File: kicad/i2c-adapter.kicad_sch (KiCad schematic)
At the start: 40 parts, among them J1 Conn_02x13_Top_Bottom, J10 AUX IN, J11 +5V, J2 I2C-1, J3 I2C-2, J4 I2C-3R, J5 I2C-4R, J6 SPI-1, J7 SPI-2, J8 SPI-3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

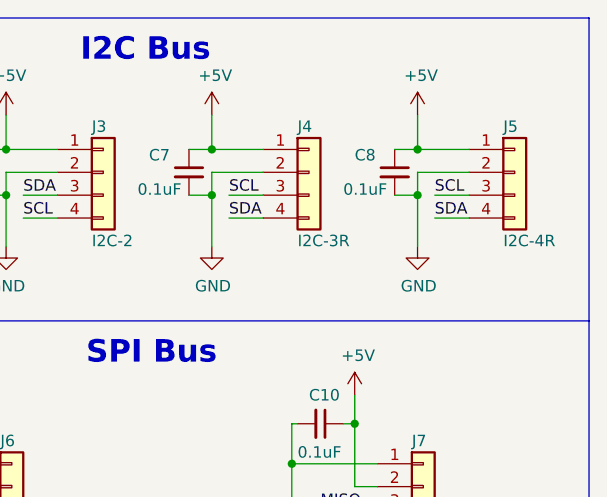
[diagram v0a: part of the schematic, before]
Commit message: Cleaned up PCB routes and positions; Converted I2C to Adafruit standard pinout. Have Git ignore Kicad generated files.
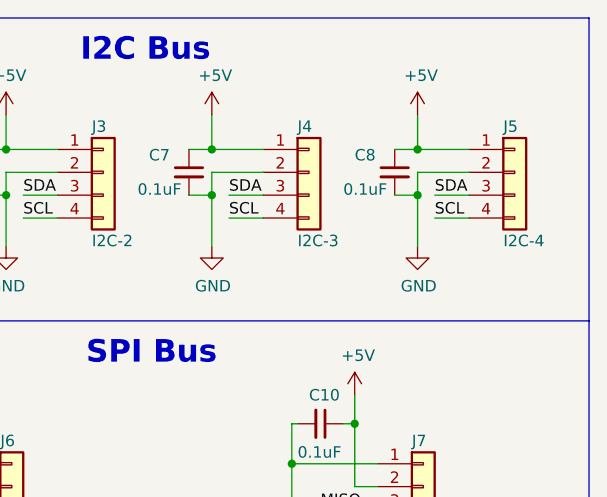
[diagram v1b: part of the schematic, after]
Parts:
- J4: value I2C-3R -> I2C-3
- J5: value I2C-4R -> I2C-4
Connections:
- net SCL: now also J4.4 (Pin_4), J5.4 (Pin_4); no longer J4.3 (Pin_3), J5.3 (Pin_3)
- net SDA: now also J4.3 (Pin_3), J5.3 (Pin_3); no longer J4.4 (Pin_4), J5.4 (Pin_4)
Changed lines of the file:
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@@
     (effects (font (size 1.27 1.27)) (justify right bottom))
   )
-  (label "SDA" (at 222.885 38.1 0)
+  (label "SCL" (at 222.885 38.1 0)
     (effects (font (size 1.27 1.27)) (justify left bottom))
   )
@@
     (effects (font (size 1.27 1.27)) (justify left bottom))
   )
-  (label "SCL" (at 245.745 35.56 0)
+  (label "SDA" (at 245.745 35.56 0)
     (effects (font (size 1.27 1.27)) (justify left bottom))
   )
@@
     (effects (font (size 1.27 1.27)) (justify left bottom))
   )
-  (label "SDA" (at 245.745 38.1 0)
+  (label "SCL" (at 245.745 38.1 0)
     (effects (font (size 1.27 1.27)) (justify left bottom))
   )
@@
     (effects (font (size 1.27 1.27)) (justify left bottom))
   )
-  (label "SCL" (at 222.885 35.56 0)
+  (label "SDA" (at 222.885 35.56 0)
     (effects (font (size 1.27 1.27)) (justify left bottom))
   )
@@
       (effects (font (size 1.27 1.27)) (justify left))
     )
-    (property "Value" "I2C-3R" (id 1) (at 230.505 40.64 0)
+    (property "Value" "I2C-3" (id 1) (at 230.505 40.64 0)
       (effects (font (size 1.27 1.27)) (justify left))
     )
@@
       (effects (font (size 1.27 1.27)) (justify left))
     )
-    (property "Value" "I2C-4R" (id 1) (at 253.365 40.64 0)
+    (property "Value" "I2C-4" (id 1) (at 253.365 40.64 0)
       (effects (font (size 1.27 1.27)) (justify left))
     )
@@
     )
     (path "/00000000-0000-0000-0000-0000629746a0"
-      (reference "J4") (unit 1) (value "I2C-3R") (footprint "Connector_PinSocket_2.54mm:PinSocket_1x04_P2.54mm_Vertical")
+      (reference "J4") (unit 1) (value "I2C-3") (footprint "Connector_PinSocket_2.54mm:PinSocket_1x04_P2.54mm_Vertical")
     )
     (path "/4099fc80-b556-41b1-a25c-163e57c74eec"
-      (reference "J5") (unit 1) (value "I2C-4R") (footprint "Connector_PinSocket_2.54mm:PinSocket_1x04_P2.54mm_Vertical")
+      (reference "J5") (unit 1) (value "I2C-4") (footprint "Connector_PinSocket_2.54mm:PinSocket_1x04_P2.54mm_Vertical")
     )
     (path "/01501bfb-9b34-47a7-81a2-8d14c6d17642"

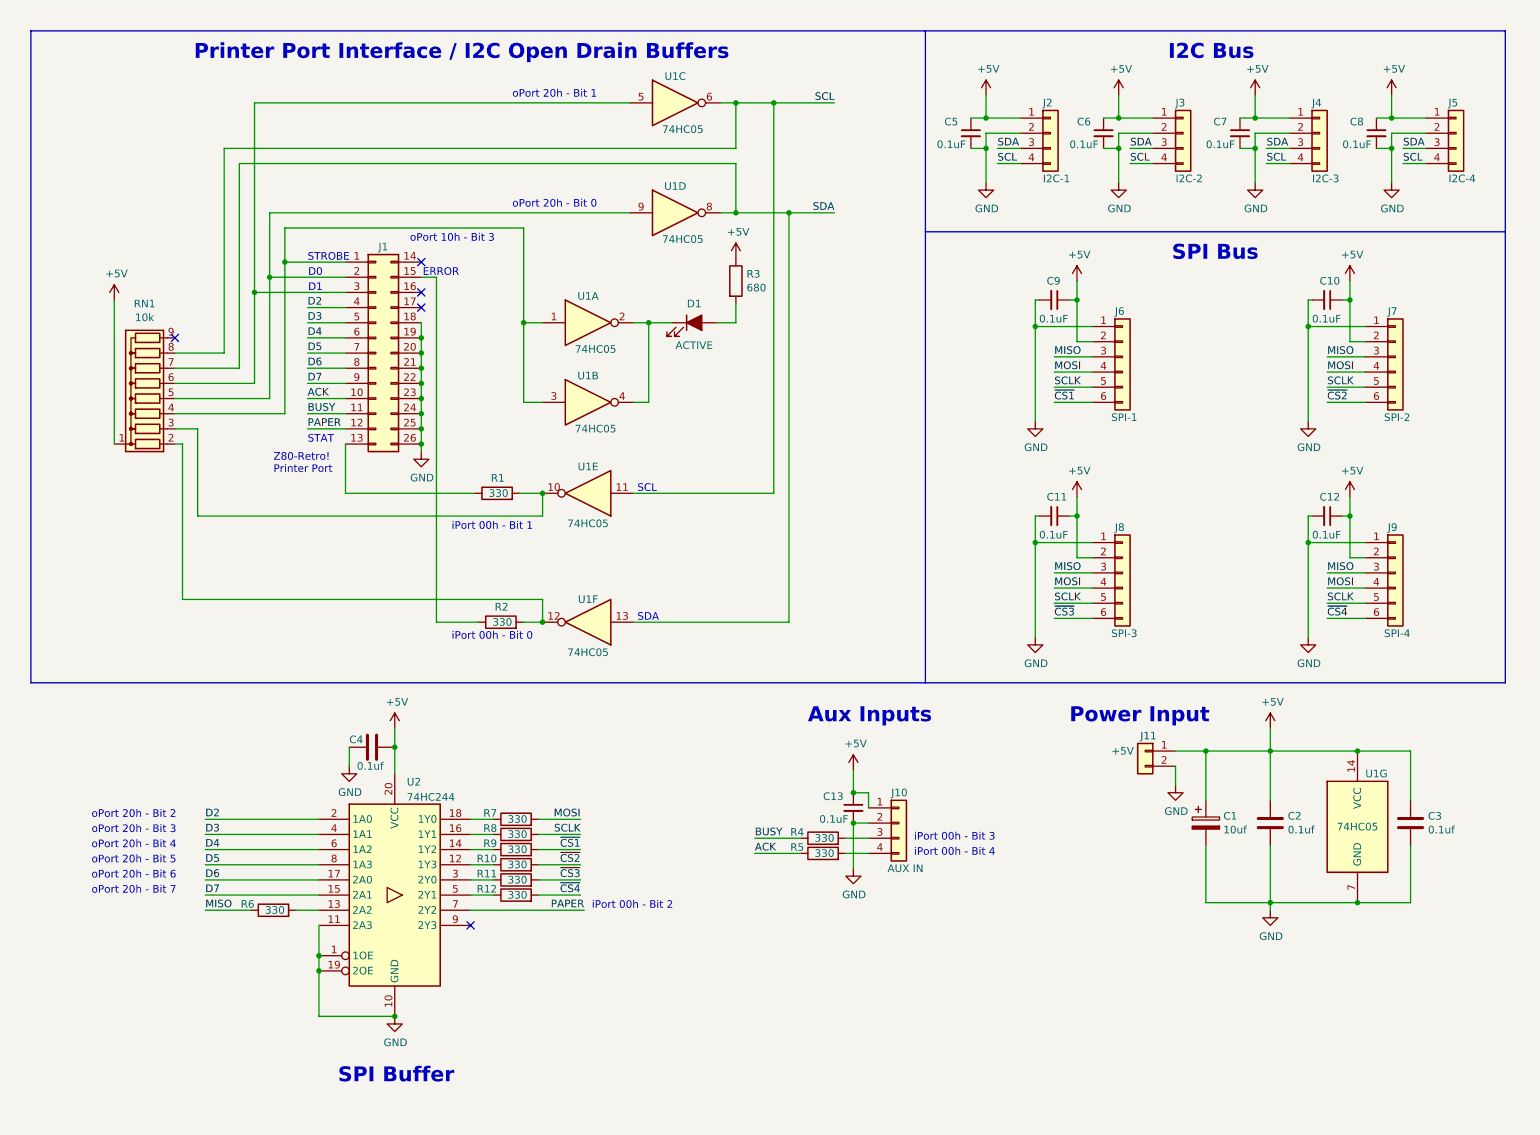
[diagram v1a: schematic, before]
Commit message: Add voltage regulator for +3.3V power; Move all SMD components to top side.
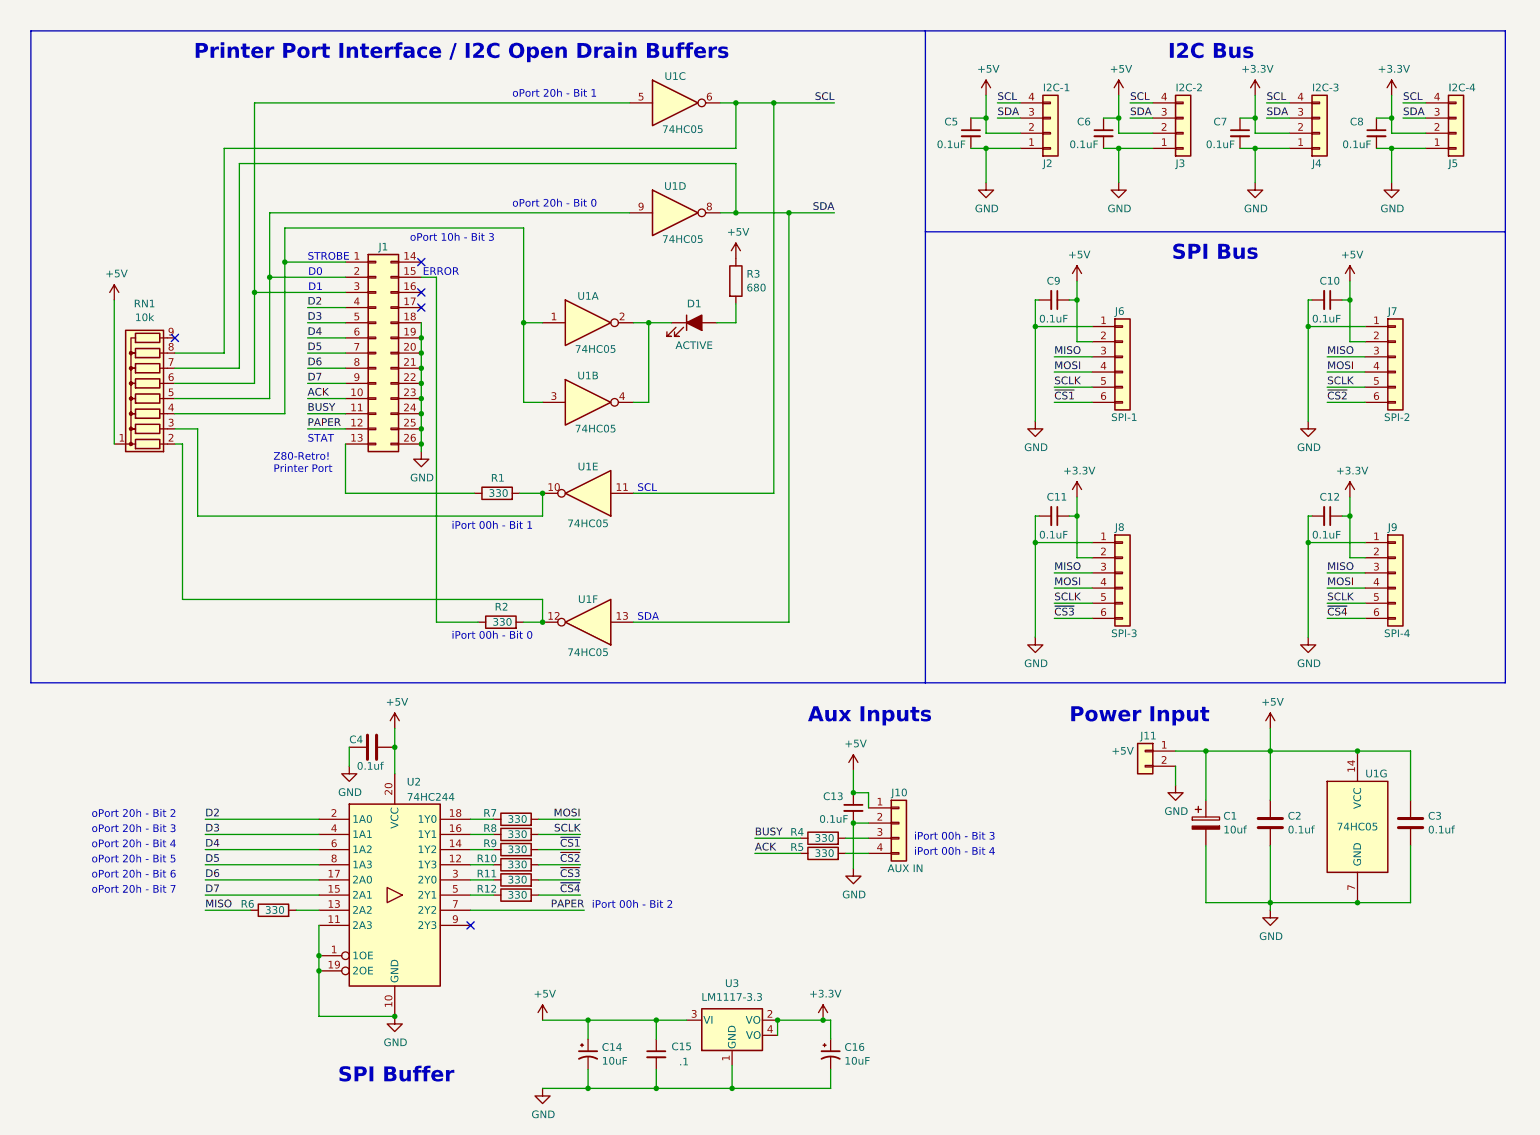
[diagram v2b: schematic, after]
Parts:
- added C14, C16: 10uF, Capacitor_SMD:C_0805_2012Metric_Pad1.18x1.45mm_HandSolder, symbol 2063-Z80-rescue:CP1_Small-Device
- added C15: .1, Capacitor_SMD:C_0805_2012Metric_Pad1.18x1.45mm_HandSolder, symbol Device:C_Small
- added U3: LM1117-3.3, digikey-footprints:SOT-223, symbol 2063-Z80-rescue:LM1117-3.3-jb-symbol
- J1: footprint jb-footprint:PinSocket_2x13_P2.54mm_Vertical_clockwise -> Connector_PinSocket_2.54mm:PinSocket_2x13_P2.54mm_Vertical
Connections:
- net +5V: now also J2.2 (Pin_2), J3.2 (Pin_2), C14.1, C15.1, U3.3 (VI); no longer C11.1, C12.1, C7.1, C8.1, J2.1 (Pin_1), J3.1 (Pin_1), J4.1 (Pin_1), J5.1 (Pin_1), J8.2 (Pin_2), J9.2 (Pin_2)
- net GND: now also J2.1 (Pin_1), J3.1 (Pin_1), J4.1 (Pin_1), J5.1 (Pin_1), C14.2, C15.2, C16.2, U3.1 (GND); no longer J2.2 (Pin_2), J3.2 (Pin_2), J4.2 (Pin_2), J5.2 (Pin_2)
- new net +3V3: C11.1, C12.1, C16.1, C7.1, C8.1, J4.2 (Pin_2), J5.2 (Pin_2), J8.2 (Pin_2), J9.2 (Pin_2), U3.2 (VO), U3.4 (VO)
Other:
- moved on the sheet: J2, J3, J4, J5

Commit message: Added BOM; Updated README to point to BOM Added JLCPCB SMD part references Specified LED characteristics (choose whichever color you want, default is RED) For jlcpcb/project.db, see https://github.com/Bouni/kicad-jlcpcb-tools Some minor Schematic and routing cleanups. Removed *_prl preferences file.  It is auto generated upon opening project.
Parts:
- C1: value 10uf -> 10uF
- C14, C16: footprint Capacitor_SMD:C_0805_2012Metric_Pad1.18x1.45mm_HandSolder -> Capacitor_Tantalum_SMD:CP_EIA-3216-10_Kemet-I_Pad1.58x1.35mm_HandSolder
- C15: value .1 -> 0.1uF
- C2, C3, C4: value 0.1uf -> 0.1uF
- D1: value ACTIVE -> 20mA 120°
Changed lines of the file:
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@@
       (effects (font (size 1.27 1.27)) (justify left))
     )
-    (property "Value" "0.1uf" (id 1) (at 249.936 149.733 0)
+    (property "Value" "0.1uF" (id 1) (at 249.936 149.733 0)
       (effects (font (size 1.27 1.27)) (justify left))
     )
@@
     (in_bom yes) (on_board yes)
     (property "Reference" "D1" (id 0) (at 127 61.595 0))
-    (property "Value" "ACTIVE" (id 1) (at 127 68.58 0))
+    (property "Value" "20mA 120°" (id 1) (at 127 68.58 0))
     (property "Footprint" "LED_SMD:LED_0805_2012Metric_Pad1.15x1.40mm_HandSolder" (id 2) (at 127 64.77 0)
       (effects (font (size 1.27 1.27)) hide)
     )
-    (property "Datasheet" "~" (id 3) (at 127 64.77 0)
+    (property "Datasheet" "https://www.amazon.com/dp/B01CUGA8JO/" (id 3) (at 127 64.77 0)
       (effects (font (size 1.27 1.27)) hide)
     )
@@
       (effects (font (size 1.27 1.27)) (justify left))
     )
-    (property "Value" "10uf" (id 1) (at 215.646 149.733 0)
+    (property "Value" "10uF" (id 1) (at 215.646 149.733 0)
       (effects (font (size 1.27 1.27)) (justify left))
     )
@@
       (effects (font (size 1.27 1.27)) (justify left))
     )
-    (property "Value" "0.1uf" (id 1) (at 226.441 149.733 0)
+    (property "Value" "0.1uF" (id 1) (at 226.441 149.733 0)
       (effects (font (size 1.27 1.27)) (justify left))
     )
@@
       (effects (font (size 1.27 1.27)) (justify left))
     )
-    (property "Footprint" "Capacitor_SMD:C_0805_2012Metric_Pad1.18x1.45mm_HandSolder" (id 2) (at 109.22 187.325 0)
+    (property "Footprint" "Capacitor_Tantalum_SMD:CP_EIA-3216-10_Kemet-I_Pad1.58x1.35mm_HandSolder" (id 2) (at 109.22 187.325 0)
       (effects (font (size 1.27 1.27)) hide)
     )
@@
       (effects (font (size 1.27 1.27)) (justify left))
     )
-    (property "Value" "0.1uf" (id 1) (at 70.485 139.065 90)
+    (property "Value" "0.1uF" (id 1) (at 70.485 139.065 90)
       (effects (font (size 1.27 1.27)) (justify left))
     )
@@
       (effects (font (size 1.27 1.27)) (justify left))
     )
-    (property "Footprint" "Capacitor_SMD:C_0805_2012Metric_Pad1.18x1.45mm_HandSolder" (id 2) (at 149.86 187.325 0)
+    (property "Footprint" "Capacitor_Tantalum_SMD:CP_EIA-3216-10_Kemet-I_Pad1.58x1.35mm_HandSolder" (id 2) (at 149.86 187.325 0)
       (effects (font (size 1.27 1.27)) hide)
     )
@@
       (effects (font (size 1.27 1.27)) (justify left))
     )
-    (property "Value" ".1" (id 1) (at 124.46 188.595 0)
+    (property "Value" "0.1uF" (id 1) (at 124.46 188.595 0)
       (effects (font (size 1.27 1.27)) (justify left))
     )
@@
     )
     (path "/00000000-0000-0000-0000-000062a0a2ab"
-      (reference "C1") (unit 1) (value "10uf") (footprint "Capacitor_Tantalum_SMD:CP_EIA-3216-10_Kemet-I_Pad1.58x1.35mm_HandSolder")
+      (reference "C1") (unit 1) (value "10uF") (footprint "Capacitor_Tantalum_SMD:CP_EIA-3216-10_Kemet-I_Pad1.58x1.35mm_HandSolder")
     )
     (path "/00000000-0000-0000-0000-000062a5dcf7"
-      (reference "C2") (unit 1) (value "0.1uf") (footprint "Capacitor_SMD:C_0805_2012Metric_Pad1.18x1.45mm_HandSolder")
+      (reference "C2") (unit 1) (value "0.1uF") (footprint "Capacitor_SMD:C_0805_2012Metric_Pad1.18x1.45mm_HandSolder")
     )
     (path "/00000000-0000-0000-0000-00006296c482"
-      (reference "C3") (unit 1) (value "0.1uf") (footprint "Capacitor_SMD:C_0805_2012Metric_Pad1.18x1.45mm_HandSolder")
+      (reference "C3") (unit 1) (value "0.1uF") (footprint "Capacitor_SMD:C_0805_2012Metric_Pad1.18x1.45mm_HandSolder")
     )
     (path "/e7403907-06d7-4178-9b0a-d1296fa9d5f8"
-      (reference "C4") (unit 1) (value "0.1uf") (footprint "Capacitor_SMD:C_0805_2012Metric_Pad1.18x1.45mm_HandSolder")
+      (reference "C4") (unit 1) (value "0.1uF") (footprint "Capacitor_SMD:C_0805_2012Metric_Pad1.18x1.45mm_HandSolder")
     )
     (path "/2a3e12e4-0c14-49f5-82c6-f0e2826034f5"
@@
     )
     (path "/7bb88749-02b6-40ef-800c-feb25e1854bd"
-      (reference "C14") (unit 1) (value "10uF") (footprint "Capacitor_SMD:C_0805_2012Metric_Pad1.18x1.45mm_HandSolder")
+      (reference "C14") (unit 1) (value "10uF") (footprint "Capacitor_Tantalum_SMD:CP_EIA-3216-10_Kemet-I_Pad1.58x1.35mm_HandSolder")
     )
     (path "/fa6bfb74-2181-4d10-a268-6d31b36d7842"
-      (reference "C15") (unit 1) (value ".1") (footprint "Capacitor_SMD:C_0805_2012Metric_Pad1.18x1.45mm_HandSolder")
+      (reference "C15") (unit 1) (value "0.1uF") (footprint "Capacitor_SMD:C_0805_2012Metric_Pad1.18x1.45mm_HandSolder")
     )
     (path "/f23c6407-15b1-4dbf-95cb-f22114ea0fec"
-      (reference "C16") (unit 1) (value "10uF") (footprint "Capacitor_SMD:C_0805_2012Metric_Pad1.18x1.45mm_HandSolder")
+      (reference "C16") (unit 1) (value "10uF") (footprint "Capacitor_Tantalum_SMD:CP_EIA-3216-10_Kemet-I_Pad1.58x1.35mm_HandSolder")
     )
     (path "/00000000-0000-0000-0000-0000629953ca"
-      (reference "D1") (unit 1) (value "ACTIVE") (footprint "LED_SMD:LED_0805_2012Metric_Pad1.15x1.40mm_HandSolder")
+      (reference "D1") (unit 1) (value "20mA 120°") (footprint "LED_SMD:LED_0805_2012Metric_Pad1.15x1.40mm_HandSolder")
     )
     (path "/00000000-0000-0000-0000-00006296f9b4"
